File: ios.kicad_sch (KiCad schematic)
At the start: 42 parts, among them Q4 BSS138PW,115, SW1 SW_SKRPABE010, SW2 SW_SKRPABE010, SW3 SW_SKRPABE010, SW4 SW_SKRPABE010, SW8 CVS-04B, U25 74LVC06ABQ

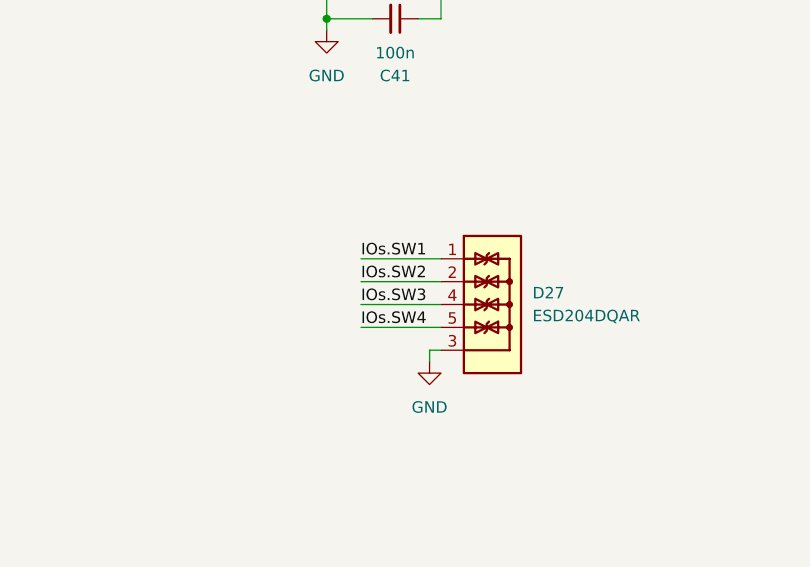
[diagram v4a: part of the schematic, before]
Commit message: [#98581] Reposition SW buttons
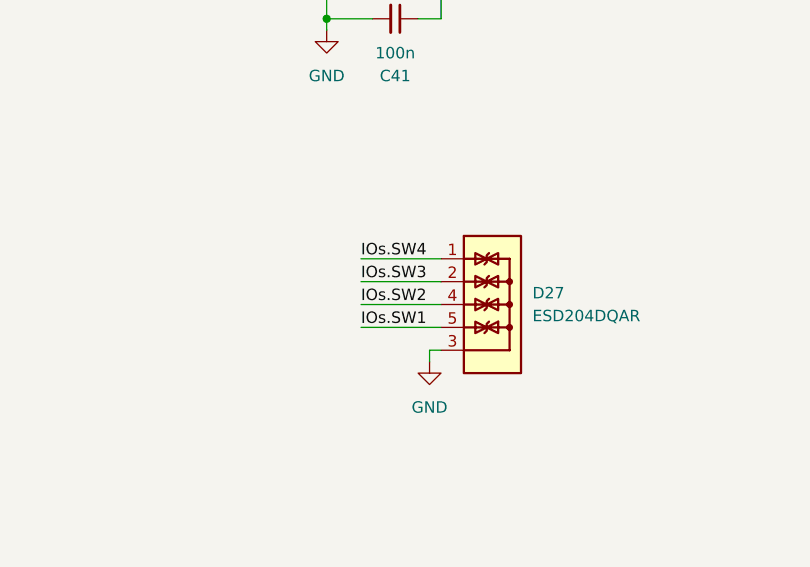
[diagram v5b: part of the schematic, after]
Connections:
- net IOs.SW1: now also D27.5, D27.6; no longer D27.1, D27.10
- net IOs.SW2: now also D27.4, D27.7; no longer D27.2, D27.9
- net IOs.SW3: now also D27.2, D27.9; no longer D27.4, D27.7
- net IOs.SW4: now also D27.1, D27.10; no longer D27.5, D27.6
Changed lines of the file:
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@@
+	)
+	(label "IOs.SW3"
+		(at 349.25 205.74 0)
+		(effects
+			(font
+				(size 1.27 1.27)
+			)
+			(justify left bottom)
+		)
 	)
 	(label "IOs.SW3"
@@
 		)
 	)
-	(label "IOs.SW3"
-		(at 349.25 208.28 0)
+	(label "IOs.SW4"
+		(at 349.25 203.2 0)
 		(effects
 			(font
@@
 		)
 	)
+	(label "IOs.SW1"
+		(at 349.25 210.82 0)
+		(effects
+			(font
+				(size 1.27 1.27)
+			)
+			(justify left bottom)
+		)
+	)
 	(label "IOs.LED1"
 		(at 71.12 52.07 180)
@@
 		)
 	)
-	(label "IOs.SW1"
-		(at 349.25 203.2 0)
-		(effects
-			(font
-				(size 1.27 1.27)
-			)
-			(justify left bottom)
-		)
-	)
 	(label "IOs.LED4_G"
 		(at 104.14 86.36 0)
@@
 		)
 	)
-	(label "IOs.SW2"
-		(at 349.25 205.74 0)
-		(effects
-			(font
-				(size 1.27 1.27)
-			)
-			(justify left bottom)
-		)
-	)
-	(label "IOs.SW4"
-		(at 349.25 210.82 0)
-		(effects
-			(font
-				(size 1.27 1.27)
-			)
-			(justify left bottom)
-		)
-	)
 	(label "IOs.LED0"
 		(at 104.14 93.98 0)
@@
 		)
 	)
+	(label "IOs.SW2"
+		(at 349.25 208.28 0)
+		(effects
+			(font
+				(size 1.27 1.27)
+			)
+			(justify left bottom)
+		)
+	)
